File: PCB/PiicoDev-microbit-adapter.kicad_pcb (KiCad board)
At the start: 2 copper layers, 59 x 30.3 mm, 15 parts, among them J1 Conn_01x40_Female, J10 Conn_01x01_Male, J2 Conn_01x04_Male, J5 Conn_01x04_Male, J6 Conn_01x01_Male, J7 Conn_01x01_Male, J8 Conn_01x01_Male, J9 Conn_01x01_Male

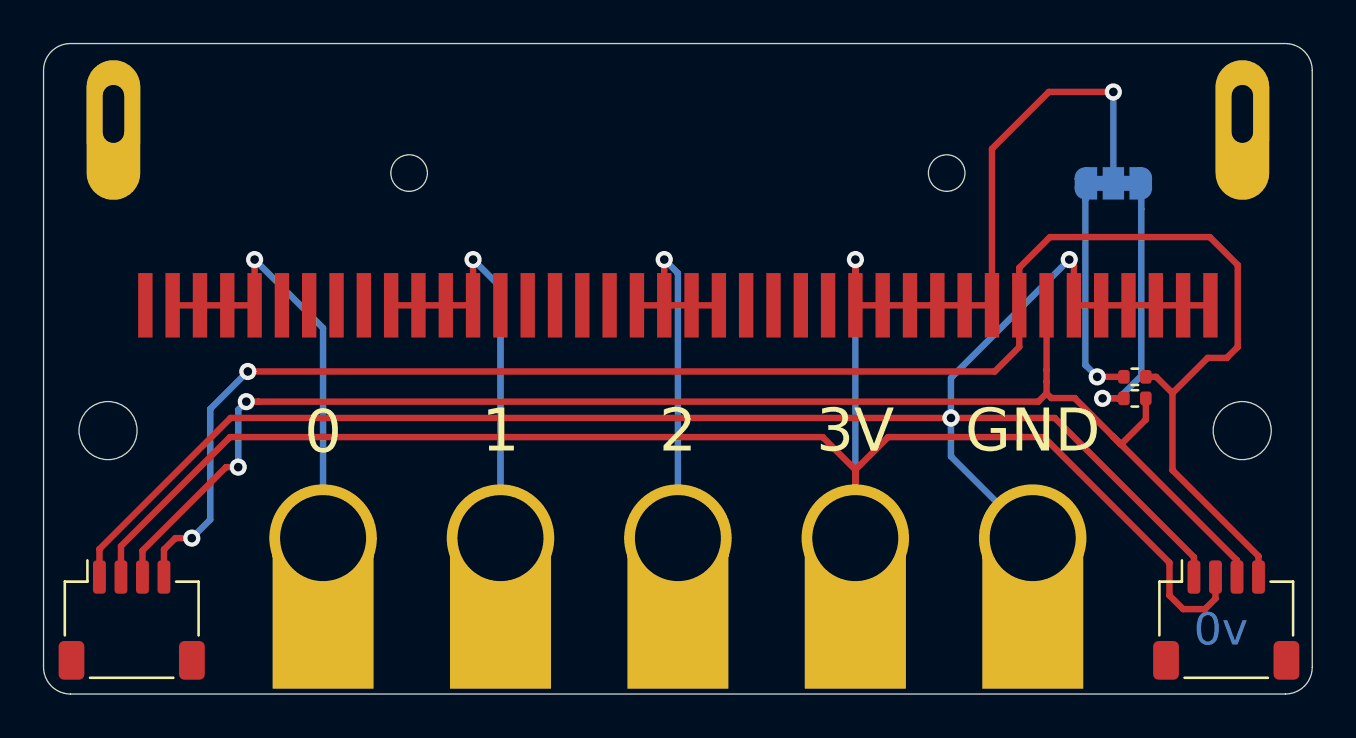
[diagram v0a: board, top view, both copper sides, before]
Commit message: v1 with premade microbit connector
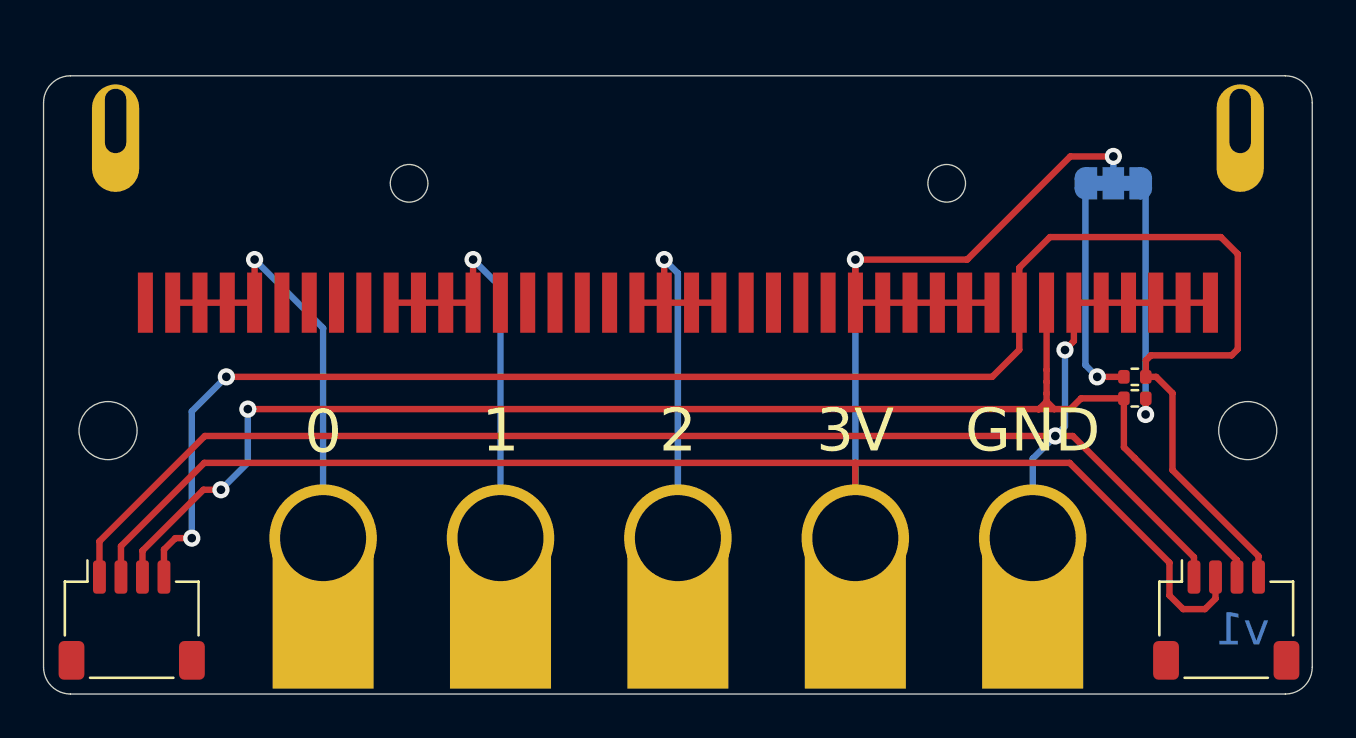
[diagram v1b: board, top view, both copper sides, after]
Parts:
- J1: footprint CoreElectronics_Components:Conn_microbit_Horizontal_SMD -> CoreElectronics_Components:Conn_microbit_Right_Angle_SMT
- moved J1 4.73 mm to (113.8, 46.4), turned to 180 degrees
- moved LOGO1 1.94 mm to (87.8, 67.3)
- moved H2 0.26 mm to (140.3, 57.9)
- turned R2 to 180 degrees
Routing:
- net +3V3: track 107.2 -> 98.9 mm
- net GND: track 83.7 -> 75.9 mm
- net /SCL: track 82.4 -> 84.7 mm
- net Net-(JP1-Pad1): track 12.2 -> 11.6 mm
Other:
- board size 59 x 30.3 mm -> 59 x 28.8 mm
- board text added: "v1"
- board text removed: "v0"

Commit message: Add Core Logo
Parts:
- added G***: LOGO, CoreElectronics_Artwork:CoreElectronics_logo_with_text_long, B.Cu at (124.5, 52.9)
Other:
- board text added: "v10"
- board text removed: "v1"

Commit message: Update artwork, bump to v11
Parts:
- removed G***: LOGO, CoreElectronics_Artwork:CoreElectronics_logo_with_text_long
- added G2: LOGO_CoreElectronics_made-with-love, CoreElectronics_Artwork:CoreElectronics_logo_5mm_v2, B.Cu at (140.2, 66.9)
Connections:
- J1 pad 15: (no net) -> Net-(J1-Pad15)
- J1 pad 16: (no net) -> Net-(J1-Pad16)
- J1 pad 17: (no net) -> Net-(J1-Pad17)
- J1 pad 18: (no net) -> Net-(J1-Pad18)
- J1 pad 23: (no net) -> Net-(J1-Pad23)
- J1 pad 24: (no net) -> Net-(J1-Pad24)
- J1 pad 25: (no net) -> Net-(J1-Pad25)
- J1 pad 26: (no net) -> Net-(J1-Pad26)
- J1 pad 27: (no net) -> Net-(J1-Pad27)
- J1 pad 32: (no net) -> Net-(J1-Pad32)
- J1 pad 33: (no net) -> Net-(J1-Pad33)
- J1 pad 34: (no net) -> Net-(J1-Pad34)
- J1 pad 35: (no net) -> Net-(J1-Pad35)
- J1 pad 40: (no net) -> Net-(J1-Pad40)
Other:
- board text added: "v11"
- board text removed: "v10"
